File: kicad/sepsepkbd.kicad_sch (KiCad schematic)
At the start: 47 parts, among them J1 Conn_01x04_Socket, J2 Conn_01x04_Socket, J4 MJ-4PP-9, SW1 SW_PUSH, SW10 SW_PUSH, SW11 SW_PUSH, SW12 SW_PUSH, SW13 SW_PUSH, SW14 SW_PUSH, SW15 SW_PUSH, SW16 SW_PUSH, SW17 SW_PUSH, SW18 SW_PUSH, SW19 SW_PUSH, SW2 SW_PUSH, SW20 SW_PUSH, SW21 SW_PUSH, SW3 SW_PUSH, SW4 SW_PUSH, SW5 SW_PUSH, SW6 SW_PUSH, SW7 SW_PUSH, SW8 SW_PUSH, SW9 SW_PUSH, U1 ProMicro

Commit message: 1.01
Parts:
- J2: footprint Connector_JST:JST_PH_S4B-PH-K_1x04_P2.00mm_Horizontal -> Connector_PinHeader_2.54mm:PinHeader_1x04_P2.54mm_Horizontal
- J3: renamed from J1; footprint Connector_JST:JST_PH_S4B-PH-K_1x04_P2.00mm_Horizontal -> Connector_PinHeader_2.54mm:PinHeader_1x04_P2.54mm_Horizontal
- renumbered J4 to J1
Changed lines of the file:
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@@
 	(title_block
 		(title "sep/sep keyboard")
-		(rev "1.00")
+		(rev "1.01")
 	)
 	(junction
@@
 		(dnp no)
 		(fields_autoplaced yes)
-		(property "Reference" "J4"
+		(property "Reference" "J1"
 			(at 224.4725 59.055 0)
 			(effects
@@
 			(project "sepsepkbd"
 				(path "/eb7c7458-55fc-48e8-93c5-5460ac0da007"
-					(reference "J4")
+					(reference "J1")
 					(unit 1)
 				)
@@
 			)
 		)
-		(property "Footprint" "Connector_JST:JST_PH_S4B-PH-K_1x04_P2.00mm_Horizontal"
+		(property "Footprint" "Connector_PinHeader_2.54mm:PinHeader_1x04_P2.54mm_Horizontal"
 			(at 87.63 72.39 0)
 			(effects
@@
 		(dnp no)
 		(fields_autoplaced yes)
-		(property "Reference" "J1"
+		(property "Reference" "J3"
 			(at 88.265 81.28 0)
 			(effects
@@
 			)
 		)
-		(property "Footprint" "Connector_JST:JST_PH_S4B-PH-K_1x04_P2.00mm_Horizontal"
+		(property "Footprint" "Connector_PinHeader_2.54mm:PinHeader_1x04_P2.54mm_Horizontal"
 			(at 87.63 91.44 0)
 			(effects
@@
 			(project "sepsepkbd"
 				(path "/eb7c7458-55fc-48e8-93c5-5460ac0da007"
-					(reference "J1")
+					(reference "J3")
 					(unit 1)
 				)

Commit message: フットプリント、シンボル追加。回路図のバージョン情報とキーボード名を変更
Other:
- title: sep/sep keyboard -> now thinking
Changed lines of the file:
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@@
 	(paper "A4")
 	(title_block
-		(title "sep/sep keyboard")
-		(rev "1.01")
+		(title "now thinking")
+		(rev "2.00")
 	)
 	(junction

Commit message: 2.1
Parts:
- removed J2, J3: Conn_01x04_Socket, Connector_PinHeader_2.54mm:PinHeader_1x04_P2.54mm_Horizontal, symbol Connector:Conn_01x04_Socket
- removed SW_RESET1: SW_PUSH, kbd:ResetSW, symbol kbd:SW_PUSH
- removed U1: ProMicro, kbd:ProMicro_v2, symbol kbd:ProMicro
- added D19: D, kbd:D3_SMD, symbol Device:D
- added J2: MJ-4PP-9, kbd:MJ-4PP-9_1side, symbol kbd:MJ-4PP-9
- added J3, J4, J5: Conn_01x10_Pin, Connector_PinHeader_2.54mm:PinHeader_1x10_P2.54mm_Vertical, symbol Connector:Conn_01x10_Pin
- added J6, J7: Conn_01x08_Pin, Connector_PinHeader_2.54mm:PinHeader_1x08_P2.54mm_Vertical, symbol Connector:Conn_01x08_Pin
- added SW19: SW_PUSH, kbd:ResetSW, symbol kbd:SW_PUSH
- added U1, U2: RP2040-Zero, isw-kbd:RP2040-Zero-THT, symbol isw-mcu:RP2040-Zero
- D20: renamed from D19; footprint kbd:D3_SMD -> kbd:D3_SMD_v2
- D21: renamed from D20; footprint kbd:D3_SMD -> kbd:D3_SMD_v2
- D22: renamed from D21; footprint kbd:D3_SMD -> kbd:D3_SMD_v2
- J1: footprint kbd:MJ-4PP-9 -> kbd:MJ-4PP-9_1side
- SW1, SW10, SW11, SW12, SW13, SW14, SW15, SW16, SW17, SW18, SW2, SW3, SW4, SW5, SW6, SW7, SW8, SW9: footprint keyswitches:SW_PG1350_reversible -> keyswitches:Kailh_socket_PG1350_reversible
- SW20: renamed from SW19; footprint keyswitches:SW_PG1350_reversible -> keyswitches:Kailh_socket_PG1350
- SW21: renamed from SW20; footprint keyswitches:SW_PG1350_reversible -> keyswitches:Kailh_socket_PG1350
- SW22: renamed from SW21; footprint keyswitches:SW_PG1350_reversible -> keyswitches:Kailh_socket_PG1350
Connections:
- net GND: now also J2.C, J6.2 (Pin_2), J7.2 (Pin_2), U1.31 (GND), U2.31 (GND)
- net data: now also J2.B, U1.0, U2.0
- net bu1_col4: now reaches SW20.1
- net bu1_col4: now also J4.8 (Pin_8), J5.8 (Pin_8), U1.5, U2.5
- net bu1_row3: now reaches D20.1 (K), D21.1 (K), D22.1 (K)
- net bu1_row3: now also U1.26, U2.26
- net bu1_col6: now reaches SW22.1
- net bu1_col6: now also J4.10 (Pin_10), J5.10 (Pin_10), U1.7, U2.7
- net bu1_col5: now reaches SW21.1
- net bu1_col5: now also J4.9 (Pin_9), J5.9 (Pin_9), U1.6, U2.6
- net VCC renamed u1_3.3v
- net u1_3.3v: now also J6.3 (Pin_3), U1.30 (3V3)
- net col0 renamed t_col0
- net t_col0: now also J3.4 (Pin_4)
- net col1 renamed t_col1
- net t_col1: now also J3.5 (Pin_5)
- net col2 renamed t_col2
- net t_col2: now also J3.6 (Pin_6)
- net col3 renamed t_col3
- net t_col3: now also J3.7 (Pin_7)
- net col4 renamed t_col4
- net t_col4: now also J3.8 (Pin_8)
- net col5 renamed t_col5
- net t_col5: now also J3.9 (Pin_9)
- net row0 renamed t_row0
- net t_row0: now also J3.1 (Pin_1)
- net row1 renamed t_row1
- net t_row1: now also J3.2 (Pin_2)
- net row2 renamed t_row2
- net t_row2: now also D19.1 (K), J3.3 (Pin_3)
- new net: D19.2 (A), SW19.2
- new net bu1_5v: J6.1 (Pin_1), U1.32 (5V)
- new net bu1_col0: J4.4 (Pin_4), U1.1
- new net bu1_col1: J4.5 (Pin_5), U1.2
- new net bu1_col2: J4.6 (Pin_6), U1.3
- new net bu1_col3: J4.7 (Pin_7), U1.4
- new net bu1_op1: J6.4 (Pin_4), U1.9
- new net bu1_op2: J6.5 (Pin_5), U1.10
- new net bu1_op3: J6.6 (Pin_6), U1.11
- new net bu1_op4: J6.7 (Pin_7), U1.12
- new net bu1_op5: J6.8 (Pin_8), U1.13
- new net bu1_row0: J4.1 (Pin_1), U1.29
- new net bu1_row1: J4.2 (Pin_2), U1.28
- new net bu1_row2: J4.3 (Pin_3), U1.27
- new net bu2_5v: J7.1 (Pin_1), U2.32 (5V)
- new net bu2_col0: J5.4 (Pin_4), U2.1
- new net bu2_col1: J5.5 (Pin_5), U2.2
- new net bu2_col2: J5.6 (Pin_6), U2.3
- new net bu2_col3: J5.7 (Pin_7), U2.4
- new net bu2_op1: J7.4 (Pin_4), U2.9
- new net bu2_op2: J7.5 (Pin_5), U2.10
- new net bu2_op3: J7.6 (Pin_6), U2.11
- new net bu2_op4: J7.7 (Pin_7), U2.12
- new net bu2_op5: J7.8 (Pin_8), U2.13
- new net bu2_row0: J5.1 (Pin_1), U2.29
- new net bu2_row1: J5.2 (Pin_2), U2.28
- new net bu2_row2: J5.3 (Pin_3), U2.27
- new net t_col6: J3.10 (Pin_10), SW19.1
- new net u2_3.3v: J2.D, J7.3 (Pin_3), U2.30 (3V3)
- no-connect marks 9 -> 8
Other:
- moved on the sheet: D1, D10, D11, D12, D13, D14, D15, D16, D17, D18, D2, D20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

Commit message: sep sep -> sprout bird
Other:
- title: now thinking -> Sprout bird
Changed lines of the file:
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@@
 	(paper "A4")
 	(title_block
-		(title "now thinking")
+		(title "Sprout bird")
 		(rev "2.00")
 	)

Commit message: 2.03
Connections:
- net data renamed u1_data
- net u1_data: no longer J2.B, U2.0
- new net u2_data: J2.B, U2.0
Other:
- title: Sprout bird -> yubino hara
- moved on the sheet: U2
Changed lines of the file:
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@@
 	(paper "A4")
 	(title_block
-		(title "Sprout bird")
-		(rev "2.00")
+		(title "yubino hara")
+		(rev "2.x")
 	)
 	(junction
@@
 	)
 	(no_connect
-		(at 96.52 153.67)
+		(at 97.79 153.67)
 	)
 	(no_connect
-		(at 71.12 153.67)
+		(at 72.39 153.67)
 	)
 	(no_connect
@@
 	)
 	(no_connect
-		(at 71.12 151.13)
+		(at 72.39 151.13)
 	)
 	(no_connect
@@
 	(wire
 		(pts
+			(xy 82.55 158.75) (xy 81.28 158.75)
+		)
+		(stroke
+			(width 0)
+			(type default)
+		)
+	)
+	(wire
+		(pts
 			(xy 93.98 54.61) (xy 93.98 58.42)
 		)
@@
 	(wire
 		(pts
+			(xy 90.17 158.75) (xy 88.9 158.75)
+		)
+		(stroke
+			(width 0)
+			(type default)
+		)
+	)
+	(wire
+		(pts
 			(xy 71.12 54.61) (xy 71.12 69.85)
 		)
@@
 	(wire
 		(pts
-			(xy 60.96 135.89) (xy 71.12 135.89)
+			(xy 62.23 135.89) (xy 72.39 135.89)
 		)
 		(stroke
@@
 	(wire
 		(pts
-			(xy 60.96 129.54) (xy 60.96 135.89)
+			(xy 62.23 129.54) (xy 62.23 135.89)
 		)
 		(stroke
@@
 	(wire
 		(pts
+			(xy 85.09 158.75) (xy 83.82 158.75)
+		)
+		(stroke
+			(width 0)
+			(type default)
+		)
+	)
+	(wire
+		(pts
 			(xy 99.06 54.61) (xy 99.06 69.85)
 		)
@@
 	(wire
 		(pts
+			(xy 87.63 158.75) (xy 86.36 158.75)
+		)
+		(stroke
+			(width 0)
+			(type default)
+		)
+	)
+	(wire
+		(pts
 			(xy 93.98 58.42) (xy 66.04 58.42)
 		)
@@
 	(wire
 		(pts
+			(xy 80.01 158.75) (xy 78.74 158.75)
+		)
+		(stroke
+			(width 0)
+			(type default)
+		)
+	)
+	(wire
+		(pts
 			(xy 149.86 58.42) (xy 177.8 58.42)
 		)
@@
 	(global_label "bu2_col6"
 		(shape input)
-		(at 96.52 151.13 0)
+		(at 97.79 151.13 0)
 		(fields_autoplaced yes)
 		(effects
@@
 		)
 		(property "Intersheetrefs" "${INTERSHEET_REFS}"
-			(at 108.0926 151.13 0)
+			(at 109.3626 151.13 0)
 			(effects
 				(font
@@
 	(global_label "bu2_col3"
 		(shape input)
-		(at 96.52 143.51 0)
+		(at 97.79 143.51 0)
 		(fields_autoplaced yes)
 		(effects
@@
 		)
 		(property "Intersheetrefs" "${INTERSHEET_REFS}"
-			(at 108.0926 143.51 0)
+			(at 109.3626 143.51 0)
 			(effects
 				(font
@@
 	(global_label "u2_3.3v"
 		(shape input)
-		(at 71.12 138.43 180)
+		(at 72.39 138.43 180)
 		(fields_autoplaced yes)
 		(effects
@@
 		)
 		(property "Intersheetrefs" "${INTERSHEET_REFS}"
-			(at 60.8173 138.43 0)
+			(at 62.0873 138.43 0)
 			(effects
 				(font
@@
 	(global_label "bu2_row2"
 		(shape input)
-		(at 71.12 146.05 180)
+		(at 72.39 146.05 180)
 		(fields_autoplaced yes)
 		(effects
@@
 		)
 		(property "Intersheetrefs" "${INTERSHEET_REFS}"
-			(at 59.1845 146.05 0)
+			(at 60.4545 146.05 0)
 			(effects
 				(font
@@
 	(global_label "bu2_col5"
 		(shape input)
-		(at 96.52 148.59 0)
+		(at 97.79 148.59 0)
 		(fields_autoplaced yes)
 		(effects
@@
 		)
 		(property "Intersheetrefs" "${INTERSHEET_REFS}"
-			(at 108.0926 148.59 0)
+			(at 109.3626 148.59 0)
 			(effects
 				(font
@@
 	(global_label "bu2_row0"
 		(shape input)
-		(at 71.12 140.97 180)
+		(at 72.39 140.97 180)
 		(fields_autoplaced yes)
 		(effects
@@
 		)
 		(property "Intersheetrefs" "${INTERSHEET_REFS}"
-			(at 59.1845 140.97 0)
+			(at 60.4545 140.97 0)
 			(effects
 				(font
@@
 	(global_label "bu2_5v"
 		(shape input)
-		(at 71.12 133.35 180)
+		(at 72.39 133.35 180)
 		(fields_autoplaced yes)
 		(effects
@@
 		)
 		(property "Intersheetrefs" "${INTERSHEET_REFS}"
-			(at 61.4826 133.35 0)
+			(at 62.7526 133.35 0)
 			(effects
 				(font
@@
 	(global_label "bu2_row1"
 		(shape input)
-		(at 71.12 143.51 180)
+		(at 72.39 143.51 180)
 		(fields_autoplaced yes)
 		(effects
@@
 		)
 		(property "Intersheetrefs" "${INTERSHEET_REFS}"
-			(at 59.1845 143.51 0)
+			(at 60.4545 143.51 0)
 			(effects
 				(font
@@
 		)
 	)
-	(global_label "data"
+	(global_label "u2_data"
 		(shape input)
 		(at 88.9 193.04 0)
@@
 		)
 		(property "Intersheetrefs" "${INTERSHEET_REFS}"
-			(at 96.0579 193.04 0)
+			(at 99.384 193.04 0)
 			(effects
 				(font
@@
 		)
 	)
-	(global_label "data"
+	(global_label "u1_data"
 		(shape input)
 		(at 35.56 193.04 0)
@@
 		)
 		(property "Intersheetrefs" "${INTERSHEET_REFS}"
-			(at 42.7179 193.04 0)
+			(at 46.044 193.04 0)
 			(effects
 				(font
@@
 	(global_label "bu2_col2"
 		(shape input)
-		(at 96.52 140.97 0)
+		(at 97.79 140.97 0)
 		(fields_autoplaced yes)
 		(effects
@@
 		)
 		(property "Intersheetrefs" "${INTERSHEET_REFS}"
-			(at 108.0926 140.97 0)
+			(at 109.3626 140.97 0)
 			(effects
 				(font
@@
 	(global_label "bu2_col1"
 		(shape input)
-		(at 96.52 138.43 0)
+		(at 97.79 138.43 0)
 		(fields_autoplaced yes)
 		(effects
@@
 		)
 		(property "Intersheetrefs" "${INTERSHEET_REFS}"
-			(at 108.0926 138.43 0)
+			(at 109.3626 138.43 0)
 			(effects
 				(font
@@
 		)
 	)
-	(global_label "data"
+	(global_label "u1_data"
 		(shape input)
 		(at 49.53 132.08 0)
@@
 		)
 		(property "Intersheetrefs" "${INTERSHEET_REFS}"
-			(at 56.6879 132.08 0)
+			(at 60.014 132.08 0)
 			(effects
 				(font
@@
 	(global_label "bu2_row3"
 		(shape input)
-		(at 71.12 148.59 180)
+		(at 72.39 148.59 180)
 		(fields_autoplaced yes)
 		(effects
@@
 		)
 		(property "Intersheetrefs" "${INTERSHEET_REFS}"
-			(at 59.1845 148.59 0)
+			(at 60.4545 148.59 0)
 			(effects
 				(font
@@
 	(global_label "bu2_col0"
 		(shape input)
-		(at 96.52 135.89 0)
+		(at 97.79 135.89 0)
 		(fields_autoplaced yes)
 		(effects
@@
 		)
 		(property "Intersheetrefs" "${INTERSHEET_REFS}"
-			(at 108.0926 135.89 0)
+			(at 109.3626 135.89 0)
 			(effects
 				(font
@@
 	(global_label "bu2_col4"
 		(shape input)
-		(at 96.52 146.05 0)
+		(at 97.79 146.05 0)
 		(fields_autoplaced yes)
 		(effects
@@
 		)
 		(property "Intersheetrefs" "${INTERSHEET_REFS}"
-			(at 108.0926 146.05 0)
+			(at 109.3626 146.05 0)
 			(effects
 				(font
@@
 		)
 	)
-	(global_label "data"
+	(global_label "u2_data"
 		(shape input)
-		(at 96.52 133.35 0)
+		(at 97.79 133.35 0)
 		(fields_autoplaced yes)
 		(effects
@@
 		)
 		(property "Intersheetrefs" "${INTERSHEET_REFS}"
-			(at 103.6779 133.35 0)
+			(at 108.274 133.35 0)
 			(effects
 				(font
@@
 	(symbol
 		(lib_id "isw-mcu:RP2040-Zero")
-		(at 83.82 143.51 0)
+		(at 85.09 143.51 0)
 		(unit 1)
 		(exclude_from_sim no)
@@
 		(fields_autoplaced yes)
 		(property "Reference" "U2"
-			(at 83.82 125.73 0)
+			(at 85.09 125.73 0)
 			(effects
 				(font
@@
 		)
 		(property "Value" "RP2040-Zero"
-			(at 83.82 128.27 0)
+			(at 85.09 128.27 0)
 			(effects
 				(font
@@
 		)
 		(property "Footprint" "isw-kbd:RP2040-Zero-THT"
-			(at 83.82 128.27 0)
+			(at 85.09 128.27 0)
 			(effects
 				(font
@@
 		)
 		(property "Datasheet" ""
-			(at 83.82 128.27 0)
+			(at 85.09 128.27 0)
 			(effects
 				(font
@@
 		)
 		(property "Description" ""
-			(at 83.82 143.51 0)
+			(at 85.09 143.51 0)
 			(effects
 				(font
@@
 	(symbol
 		(lib_id "power:GND")
-		(at 60.96 129.54 180)
+		(at 62.23 129.54 180)
 		(unit 1)
 		(exclude_from_sim no)
@@
 		(fields_autoplaced yes)
 		(property "Reference" "#PWR03"
-			(at 60.96 123.19 0)
+			(at 62.23 123.19 0)
 			(effects
 				(font
@@
 		)
 		(property "Value" "GND"
-			(at 63.5 128.2699 0)
+			(at 64.77 128.2699 0)
 			(effects
 				(font
@@
 		)
 		(property "Footprint" ""
-			(at 60.96 129.54 0)
+			(at 62.23 129.54 0)
 			(effects
 				(font
@@
 		)
 		(property "Datasheet" ""
-			(at 60.96 129.54 0)
+			(at 62.23 129.54 0)
 			(effects
 				(font
@@
 		)
 		(property "Description" "Power symbol creates a global label with name \"GND\" , ground"
-			(at 60.96 129.54 0)
+			(at 62.23 129.54 0)
 			(effects
 				(font

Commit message: tmp
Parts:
- SW19: footprint kbd:ResetSW -> keyswitches:Kailh_socket_PG1350_reversible
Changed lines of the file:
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@@
 			)
 		)
-		(property "Footprint" "kbd:ResetSW"
+		(property "Footprint" "keyswitches:Kailh_socket_PG1350_reversible"
 			(at 219.71 69.85 0)
 			(effects

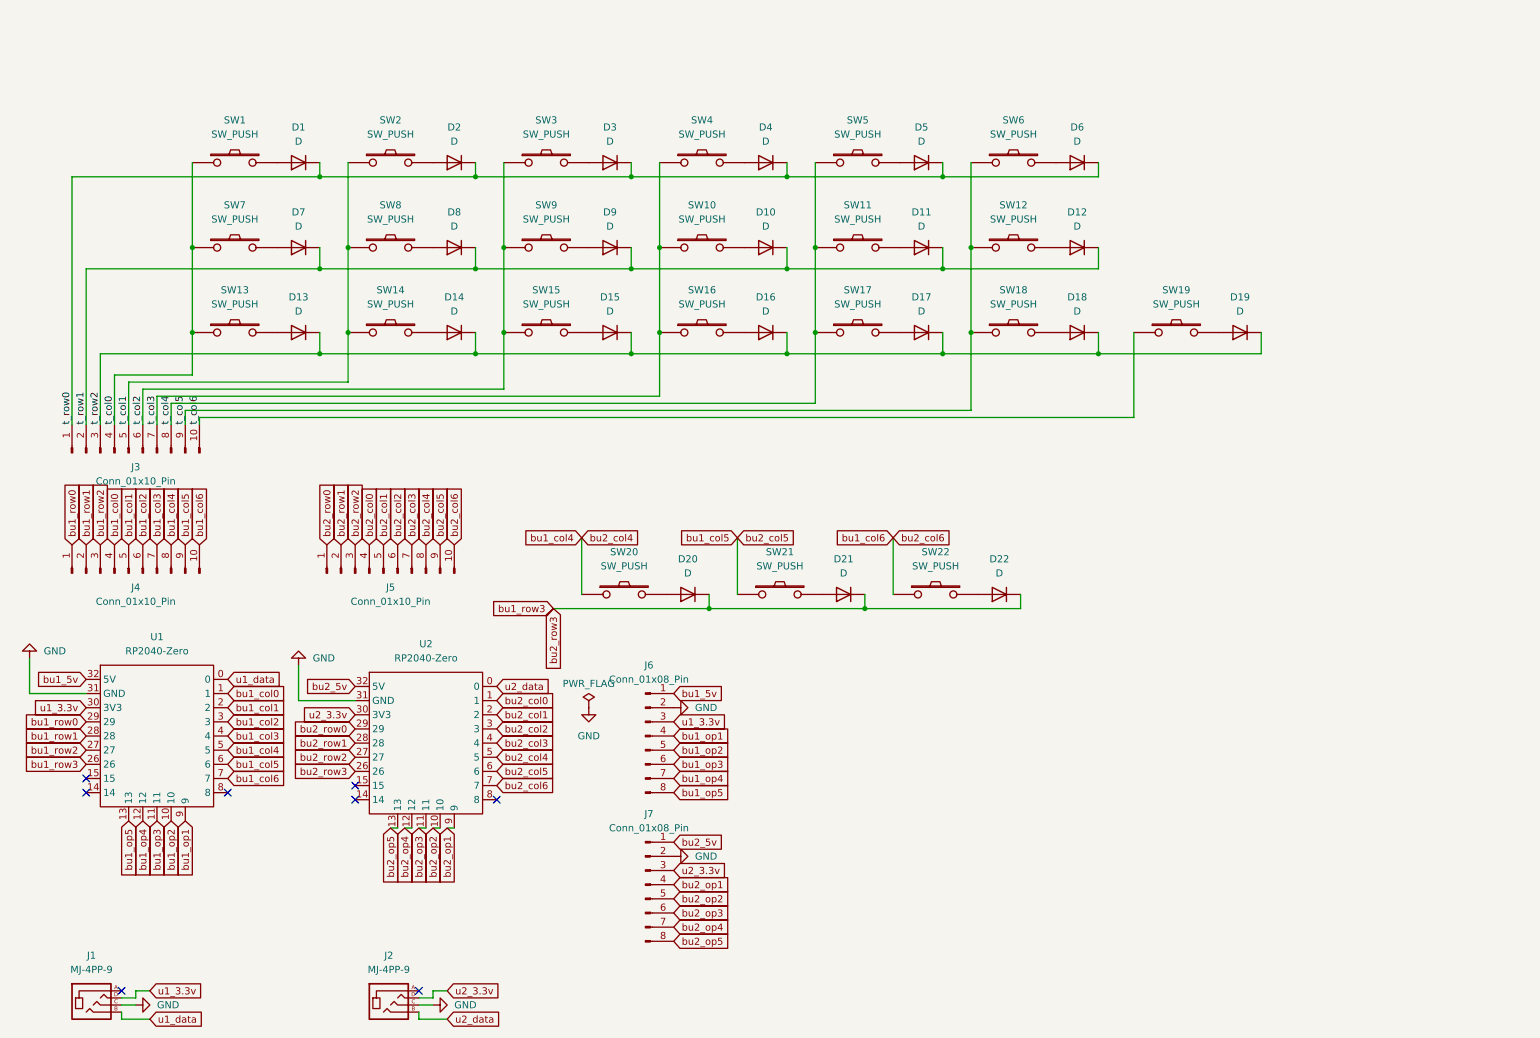
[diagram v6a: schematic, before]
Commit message: Split thumbsboard left and right.
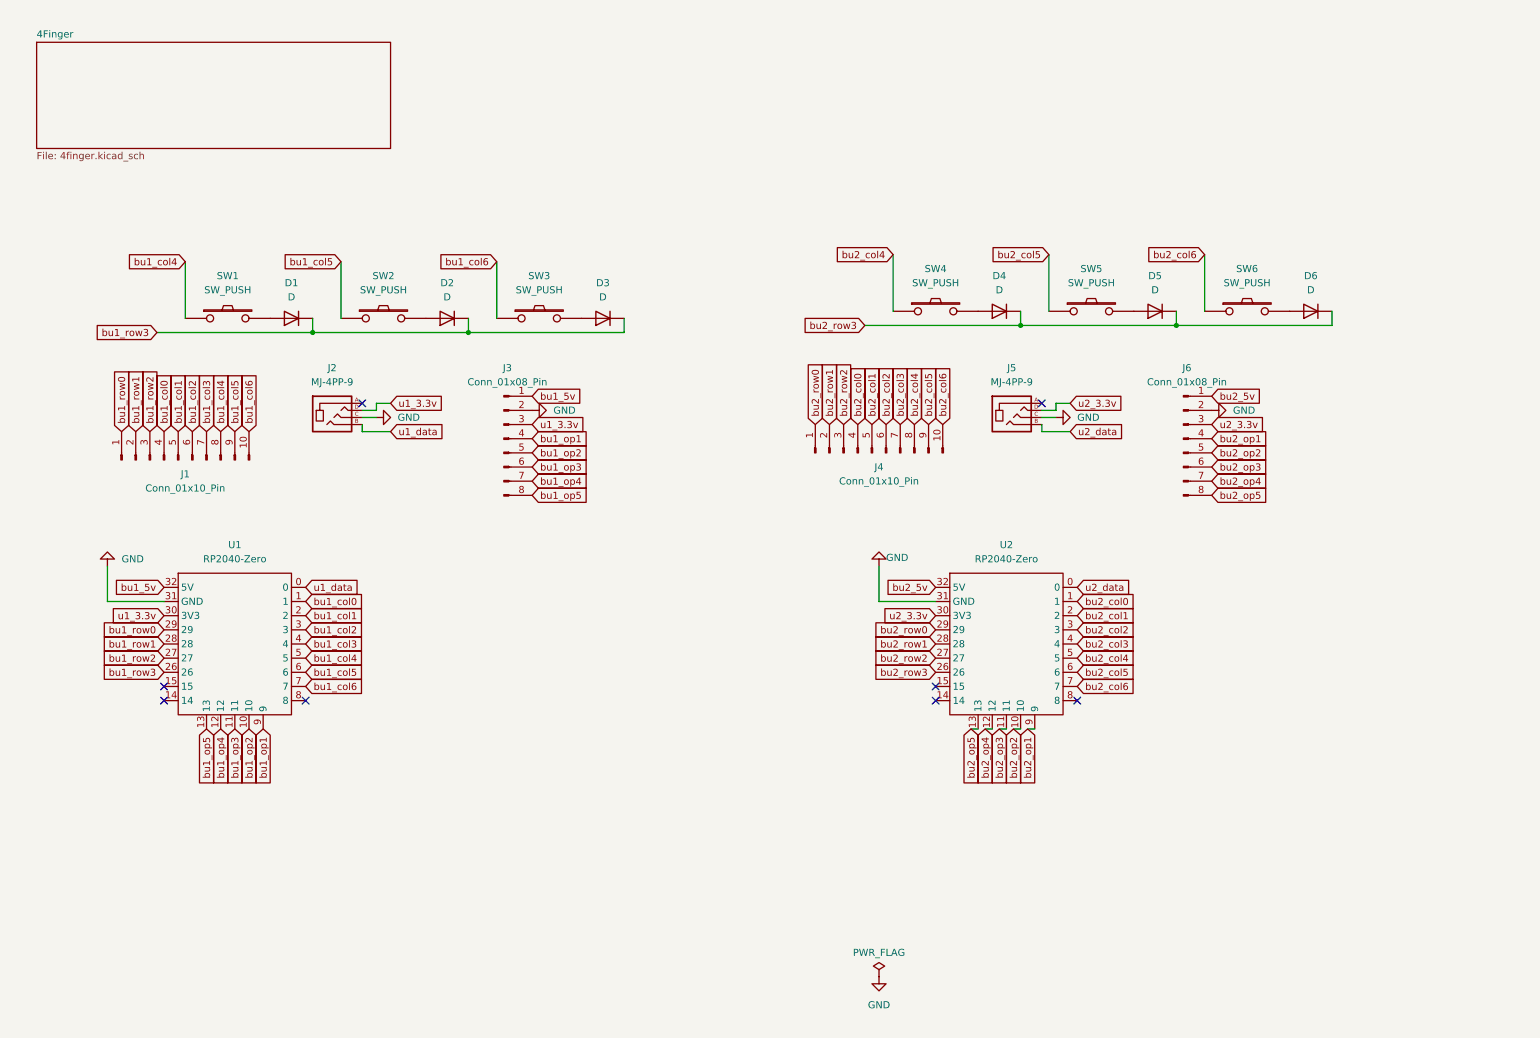
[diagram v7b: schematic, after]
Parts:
- removed D1, D10, D11, D12, D13, D14, D15, D16, D17, D18, D19, D2, D3, D7, D8, D9: D, kbd:D3_SMD, symbol Device:D
- removed J3: Conn_01x10_Pin, Connector_PinHeader_2.54mm:PinHeader_1x10_P2.54mm_Vertical, symbol Connector:Conn_01x10_Pin
- removed J7: Conn_01x08_Pin, Connector_PinHeader_2.54mm:PinHeader_1x08_P2.54mm_Vertical, symbol Connector:Conn_01x08_Pin
- removed SW1, SW10, SW11, SW12, SW13, SW14, SW15, SW16, SW17, SW18, SW19, SW2, SW3, SW7, SW8, SW9: SW_PUSH, keyswitches:Kailh_socket_PG1350_reversible, symbol kbd:SW_PUSH
- added J3: Conn_01x08_Pin, Connector_PinHeader_2.54mm:PinHeader_1x08_P2.54mm_Vertical, symbol Connector:Conn_01x08_Pin
- D4, D5, D6: footprint kbd:D3_SMD -> kbd:D3_SMD_v2
- SW4, SW5, SW6: footprint keyswitches:Kailh_socket_PG1350_reversible -> keyswitches:Kailh_socket_PG1350
- renumbered D20 to D1, D21 to D2, D22 to D3, J4 to J1, J1 to J2, J5 to J4, J2 to J5, SW20 to SW1, SW21 to SW2, SW22 to SW3
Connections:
- net GND: now also J3.2 (Pin_2)
- net bu1_5v: now also J3.1 (Pin_1); no longer J6.1 (Pin_1)
- net bu1_col4: no longer J4.8 (Pin_8), U2.5
- net bu1_col5: no longer J4.9 (Pin_9), U2.6
- net bu1_col6: no longer J4.10 (Pin_10), U2.7
- net bu1_op1: now also J3.4 (Pin_4); no longer J6.4 (Pin_4)
- net bu1_op2: now also J3.5 (Pin_5); no longer J6.5 (Pin_5)
- net bu1_op3: now also J3.6 (Pin_6); no longer J6.6 (Pin_6)
- net bu1_op4: now also J3.7 (Pin_7); no longer J6.7 (Pin_7)
- net bu1_op5: now also J3.8 (Pin_8); no longer J6.8 (Pin_8)
- net bu1_row3: no longer U2.26
- net bu2_5v: now also J6.1 (Pin_1)
- net bu2_op1: now also J6.4 (Pin_4)
- net bu2_op2: now also J6.5 (Pin_5)
- net bu2_op3: now also J6.6 (Pin_6)
- net bu2_op4: now also J6.7 (Pin_7)
- net bu2_op5: now also J6.8 (Pin_8)
- net u1_3.3v: now also J3.3 (Pin_3); no longer J6.3 (Pin_3)
- net u2_3.3v: now also J6.3 (Pin_3)
- net t_col3 renamed bu2_col4
- net bu2_col4: now also J4.8 (Pin_8), U2.5
- net t_col4 renamed bu2_col5
- net bu2_col5: now also J4.9 (Pin_9), U2.6
- net t_col5 renamed bu2_col6
- net bu2_col6: now also J4.10 (Pin_10), U2.7
- net t_row0 renamed bu2_row3
- net bu2_row3: now also U2.26
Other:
- added sheet 4Finger (4finger.kicad_sch)
- moved on the sheet: D1, D2, D3, J1, J2, J4, J5, SW1, SW2, SW3, U1, U2
